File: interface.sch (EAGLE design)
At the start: 14 parts, among them IC2 ATTINY87/167AUTOMOTIVE, U1 ISL3179EIBZ

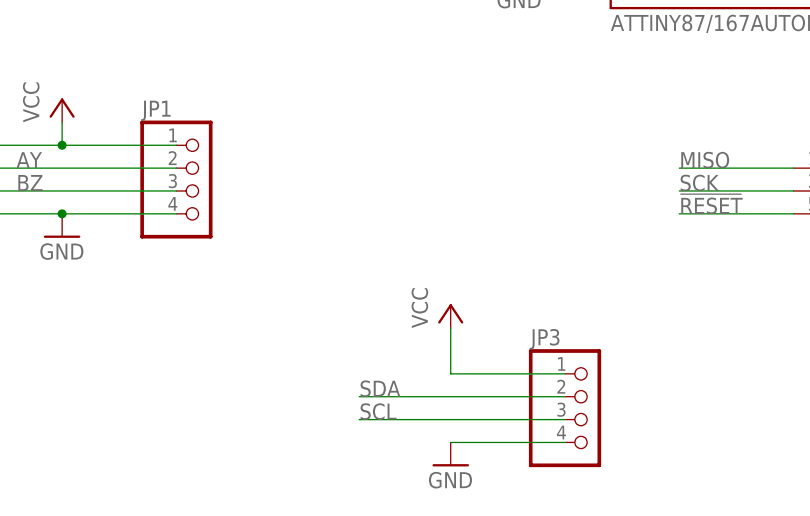
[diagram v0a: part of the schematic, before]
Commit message: forgot i2c pullups
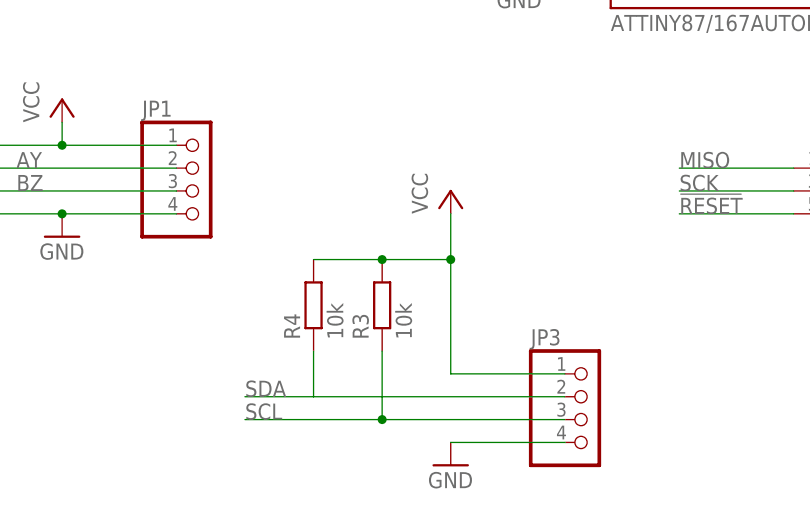
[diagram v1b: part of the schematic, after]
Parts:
- added R3, R4: 10k, resistor:R-EU_R0805
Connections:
- net SCL: now also R3.1
- net SDA: now also R4.1
- net VCC: now also R3.2, R4.2
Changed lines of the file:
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@@
 <part name="GND7" library="supply1" deviceset="GND" device=""/>
 <part name="P+7" library="glacsweb" deviceset="VCC" device=""/>
+<part name="R3" library="resistor" deviceset="R-EU_" device="R0805" value="10k"/>
+<part name="R4" library="resistor" deviceset="R-EU_" device="R0805" value="10k"/>
 </parts>
 <sheets>
@@
 <instance part="JP3" gate="A" x="114.3" y="17.78"/>
 <instance part="GND2" gate="1" x="99.06" y="12.7"/>
-<instance part="P+6" gate="VCC" x="99.06" y="30.48"/>
+<instance part="P+6" gate="VCC" x="99.06" y="43.18"/>
 <instance part="JP4" gate="A" x="241.3" y="134.62"/>
 <instance part="JP5" gate="A" x="241.3" y="116.84"/>
@@
 <instance part="GND7" gate="1" x="220.98" y="58.42"/>
 <instance part="P+7" gate="VCC" x="213.36" y="142.24"/>
+<instance part="R3" gate="G$1" x="91.44" y="30.48" rot="R90"/>
+<instance part="R4" gate="G$1" x="83.82" y="30.48" rot="R90"/>
 </instances>
 <busses>
@@
 <pinref part="P+6" gate="VCC" pin="VCC"/>
 <wire x1="111.76" y1="22.86" x2="99.06" y2="22.86" width="0.1524" layer="91"/>
-<wire x1="99.06" y1="22.86" x2="99.06" y2="27.94" width="0.1524" layer="91"/>
+<wire x1="99.06" y1="22.86" x2="99.06" y2="35.56" width="0.1524" layer="91"/>
+<pinref part="R4" gate="G$1" pin="2"/>
+<wire x1="99.06" y1="35.56" x2="99.06" y2="40.64" width="0.1524" layer="91"/>
+<wire x1="83.82" y1="35.56" x2="91.44" y2="35.56" width="0.1524" layer="91"/>
+<pinref part="R3" gate="G$1" pin="2"/>
+<junction x="91.44" y="35.56"/>
+<wire x1="91.44" y1="35.56" x2="99.06" y2="35.56" width="0.1524" layer="91"/>
+<junction x="99.06" y="35.56"/>
 </segment>
 <segment>
@@
 <segment>
 <pinref part="JP3" gate="A" pin="2"/>
-<wire x1="111.76" y1="20.32" x2="88.9" y2="20.32" width="0.1524" layer="91"/>
-<label x="88.9" y="20.32" size="1.778" layer="95"/>
+<wire x1="111.76" y1="20.32" x2="83.82" y2="20.32" width="0.1524" layer="91"/>
+<label x="76.2" y="20.32" size="1.778" layer="95"/>
+<pinref part="R4" gate="G$1" pin="1"/>
+<wire x1="83.82" y1="20.32" x2="76.2" y2="20.32" width="0.1524" layer="91"/>
+<wire x1="83.82" y1="25.4" x2="83.82" y2="20.32" width="0.1524" layer="91"/>
 </segment>
 </net>
@@
 <segment>
 <pinref part="JP3" gate="A" pin="3"/>
-<wire x1="111.76" y1="17.78" x2="88.9" y2="17.78" width="0.1524" layer="91"/>
-<label x="88.9" y="17.78" size="1.778" layer="95"/>
-</segment>
-</net>
+<wire x1="111.76" y1="17.78" x2="91.44" y2="17.78" width="0.1524" layer="91"/>
+<label x="76.2" y="17.78" size="1.778" layer="95"/>
+<pinref part="R3" gate="G$1" pin="1"/>
+<wire x1="91.44" y1="17.78" x2="76.2" y2="17.78" width="0.1524" layer="91"/>
+<wire x1="91.44" y1="25.4" x2="91.44" y2="17.78" width="0.1524" layer="91"/>
+<junction x="91.44" y="17.78"/>
+</segment>
+</net>

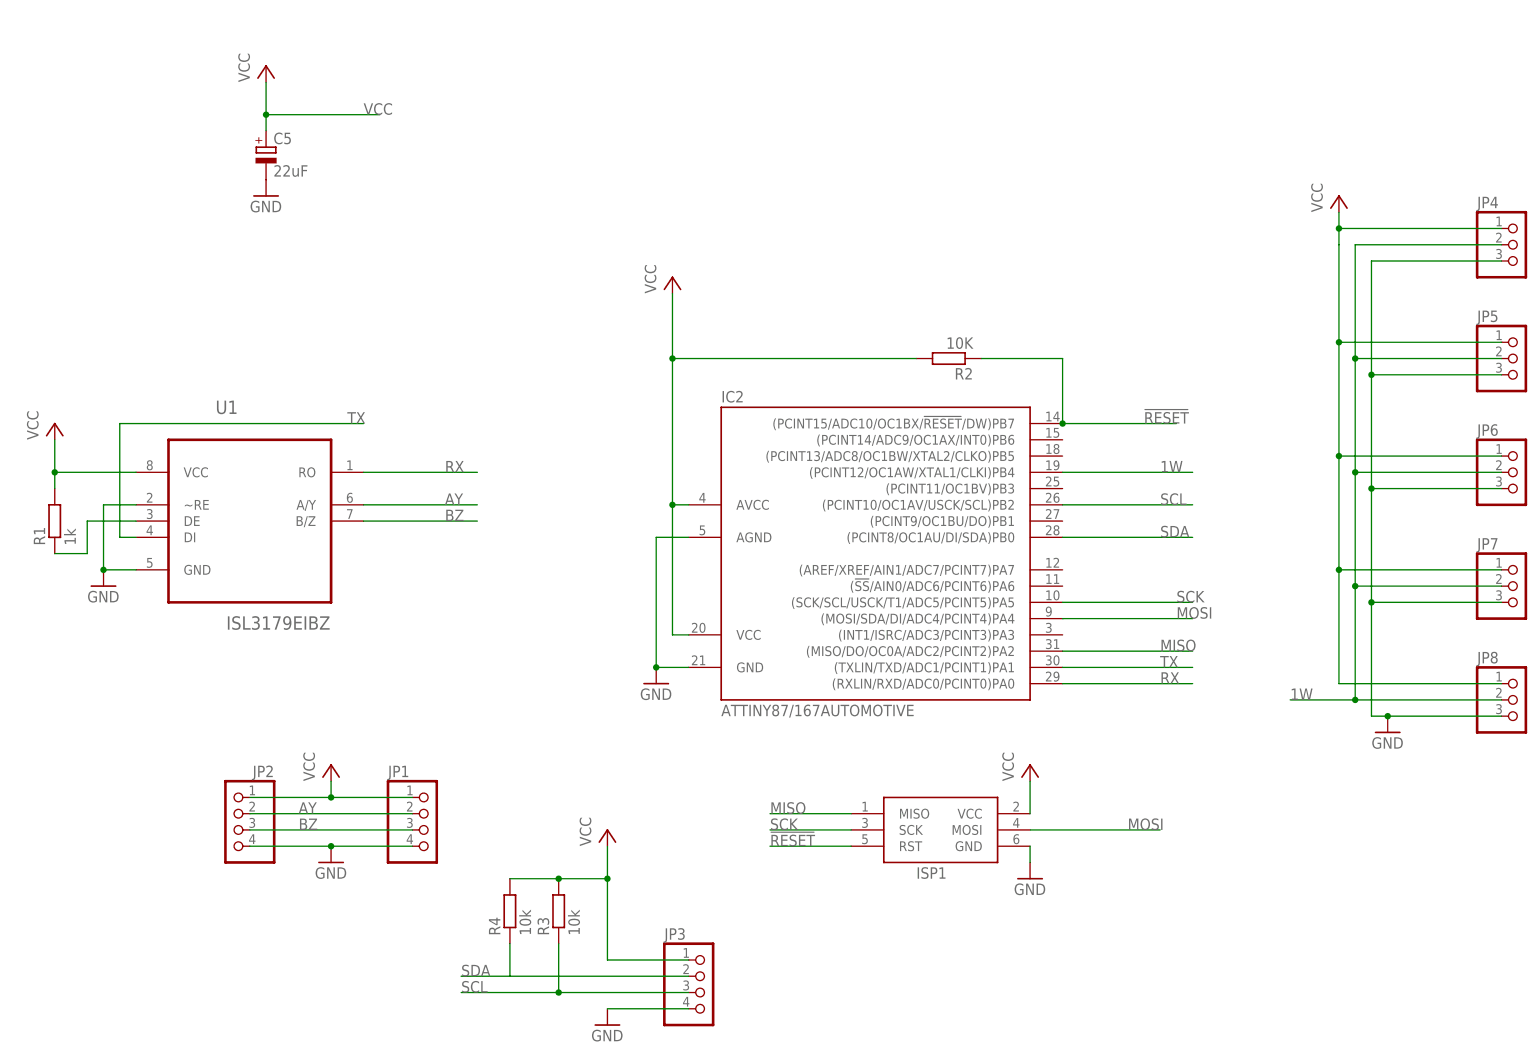
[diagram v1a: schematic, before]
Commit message: now uses an avr supported by arduino
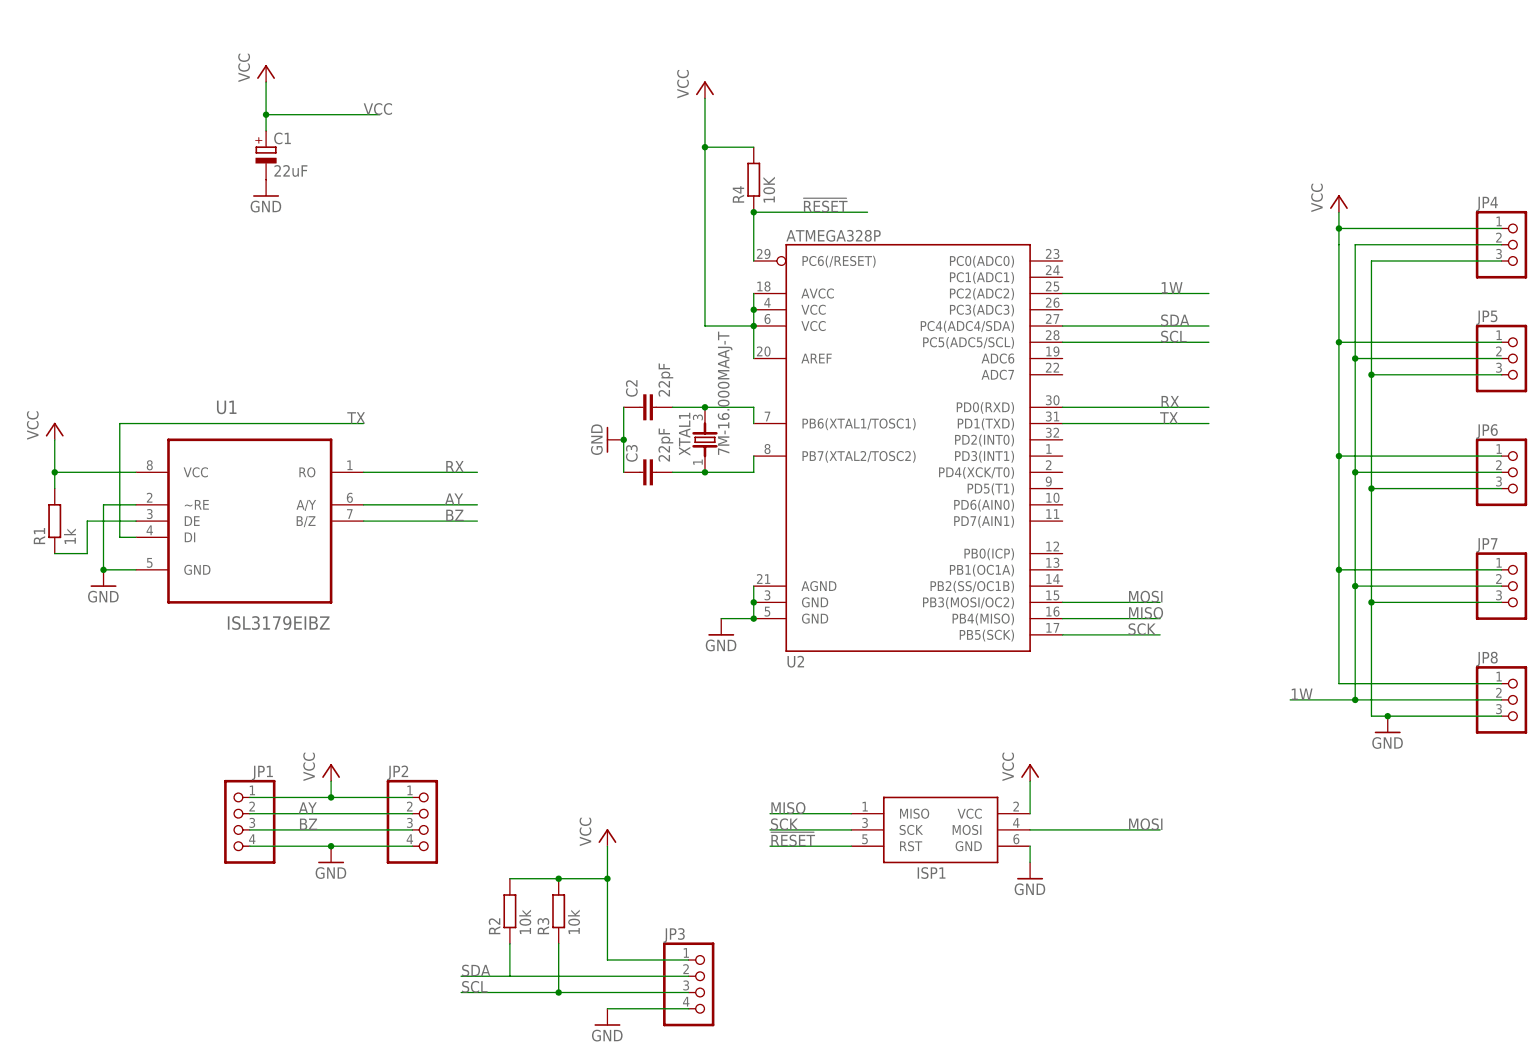
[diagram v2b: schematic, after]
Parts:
- removed IC2: ATTINY87/167AUTOMOTIVE, attiny87_167_automotive:ATTINY87/167AUTOMOTIVE
- added C2, C3: 22pF, resistor:C-EUC0805
- added U2: ATMEGA328P, SparkFun-DigitalIC:ATMEGA328_SMT
- added XTAL1: 7M-16.000MAAJ-T, TXC-7M-16.000MAAJ-T:7M-16.000MAAJ-T
- R2: value 10K -> 10k
- R4: value 10k -> 10K
- renumbered C5 to C1
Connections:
- new net N$2: C2.2, U2.PB6(XTAL1/TOSC1), XTAL1.3
- new net N$3: C3.2, U2.PB7(XTAL2/TOSC2), XTAL1.1
- net !RESET: now also R4.1, U2.PC6(/RESET); no longer IC2.(PCINT15/ADC10/OC1BX/!RESET!/DW)PB7, R2.1
- net 1W: now also U2.PC2(ADC2); no longer IC2.(PCINT12/OC1AW/XTAL1/CLKI)PB4
- net GND: now also C2.1, C3.1, U2.AGND, U2.GND@1, U2.GND@2; no longer IC2.AGND, IC2.GND
- net MISO: now also U2.PB4(MISO); no longer IC2.(MISO/DO/OC0A/ADC2/PCINT2)PA2
- net MOSI: now also U2.PB3(MOSI/OC2); no longer IC2.(MOSI/SDA/DI/ADC4/PCINT4)PA4
- net RX: now also U2.PD0(RXD); no longer IC2.(RXLIN/RXD/ADC0/PCINT0)PA0
- net SCK: now also U2.PB5(SCK); no longer IC2.(SCK/SCL/USCK/T1/ADC5/PCINT5)PA5
- net SCL: now also U2.PC5(ADC5/SCL); no longer IC2.(PCINT10/OC1AV/USCK/SCL)PB2
- net SDA: now also R2.1, U2.PC4(ADC4/SDA); no longer IC2.(PCINT8/OC1AU/DI/SDA)PB0, R4.1
- net TX: now also U2.PD1(TXD); no longer IC2.(TXLIN/TXD/ADC1/PCINT1)PA1
- net VCC: now also U2.AREF, U2.AVCC, U2.VCC@1, U2.VCC@2; no longer IC2.AVCC, IC2.VCC
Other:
- moved on the sheet: JP1, JP2, R2, R4
